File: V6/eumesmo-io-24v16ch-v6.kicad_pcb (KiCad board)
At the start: 4 copper layers, 128 x 67.8 mm, 336 parts, among them J1 250-208, J2 250-208, J3 250-208, J4 250-208, J5 250-202, J6 250-202, J7 USB_C_Receptacle_USB2.0, J8 ETHERNET, J9 250-203, Q1 WPM2015-3/TR, Q10 MMBT2222A, Q11 MMBT2222A, Q12 MMBT2222A, Q13 MMBT2222A, Q14 MMBT2222A, Q15 MMBT2222A, Q16 MMBT2222A, Q17 MMBT2222A, Q18 MMBT2222A, Q19 MMBT2222A, Q2 MMUN2211LT3G, Q3 UMH3N, Q4 MMBT2222A, Q5 MMBT2222A, Q6 MMBT2222A, Q7 MMBT2222A, Q8 MMBT2222A, Q9 MMBT2222A, SW1 RESET, SW2 1WIRE_SEL, U1 TX4138, U10 MCP23017, U11 DS2482S-100, U12 OR-3H7-4, U13 OR-3H7-4, U14 OR-3H7-4, U15 OR-3H7-4, U2 SY8089A1AAC, U3 TPS3820-33, U4 CH340K, U5 ESP32-WROOM-32UE-N16, U6 LAN8710A, U7 TPS3820-33, U8 MCP23008, U9 MCP23008

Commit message: Further improved routing between ETH jack and LAN8710A.
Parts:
- moved R35 3.09 mm to (173.0, 104.1), turned to 180 degrees
- moved R32 3.04 mm to (179.0, 104.1), turned to 0 degrees
- moved C24 1.00 mm to (179.5, 107.1)
- moved R31 0.90 mm to (179.0, 103.1), turned to 0 degrees
- moved R36 0.90 mm to (173.0, 103.1), turned to 180 degrees
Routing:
- net /LAN/ETHRXD-: track 22.8 -> 21.5 mm, vias 1 -> 2
- net +3V3A: track 42.5 -> 43.8 mm, vias 7 -> 6
- net /LAN/ETHTXD+: track 19.2 -> 18.2 mm
- net GND: track 133.3 -> 133.8 mm, vias 142 -> 140

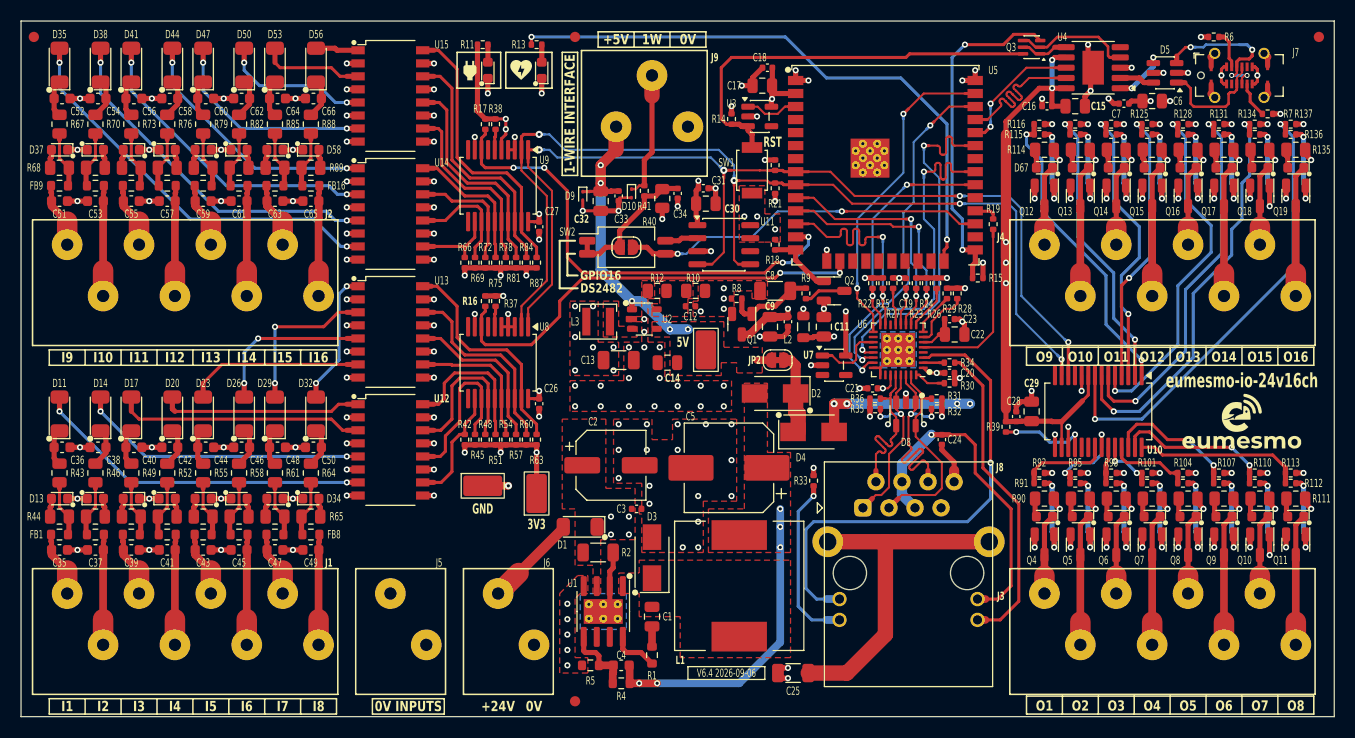
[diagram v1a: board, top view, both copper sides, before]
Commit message: Further improvements to routing between ETH jack and LAN IC.
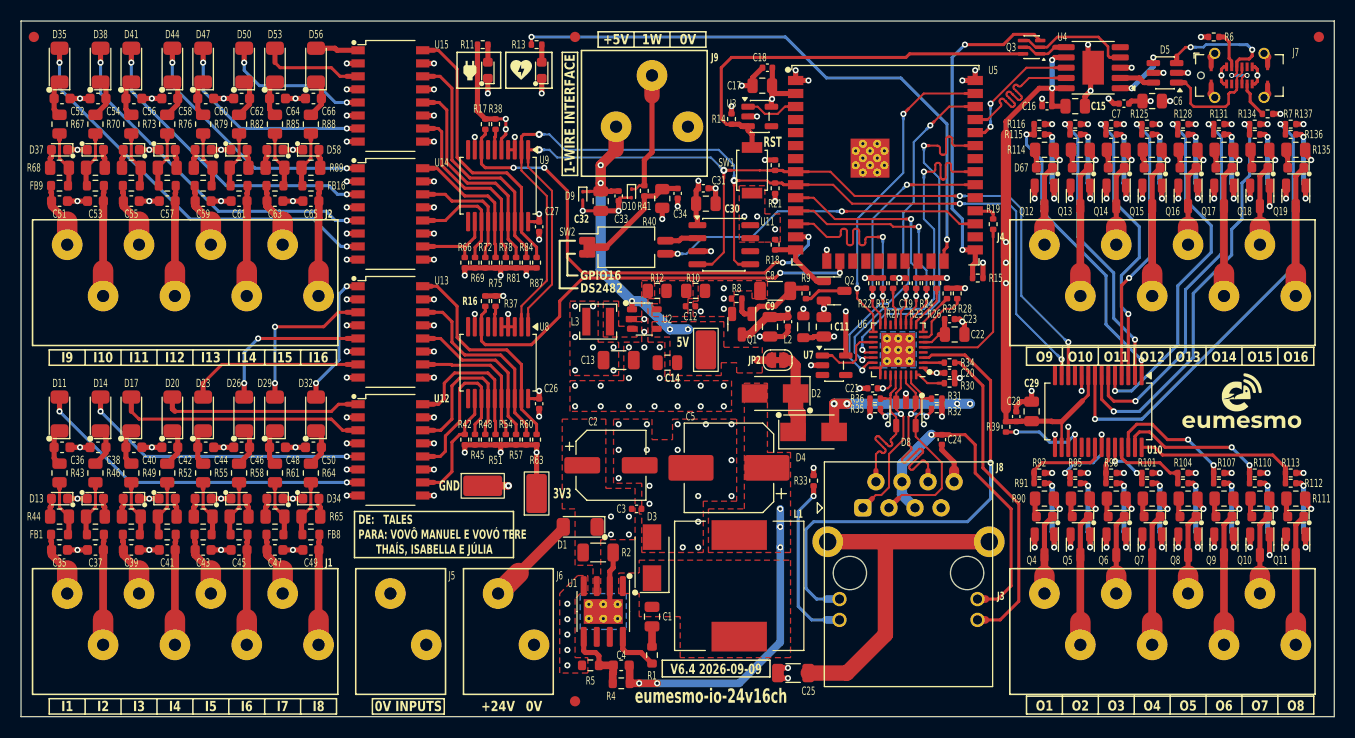
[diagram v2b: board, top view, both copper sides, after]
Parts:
- removed JP1: 1WJUMPER, Jumper:SolderJumper-2_P1.3mm_Open_RoundedPad1.0x1.5mm
- moved G*** 2.00 mm to (208.8, 103.3)
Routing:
- net /I2C Devices/1WIREGPIO: track 35.8 -> 32.4 mm
- net /I2C Devices/1WIREBUS: track 14.1 -> 13.0 mm
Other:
- board text added: "DE: TALES PARA: VOVÔ MANUEL E VOVÓ TERE THAÍS, ISABELLA E JÚLIA"
- board text added: "V6.4 2026-09-09"
- board text removed: "V6.4 2026-09-06"

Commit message: Replaced white leds for emerald.
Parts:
- D13, D16, D19, D22, D25, D28, D31, D34, D37, D40, D43, D46, D49, D52, D55, D58, D59, D6, D60, D61, D62, D63, D64, D65, D66, D67, D68, D69, D7, D70, D71, D72, D73, D74: value WHITE/0603 -> EMERALD/0603
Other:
- board text removed: "DE: TALES PARA: VOVÔ MANUEL E VOVÓ TERE THAÍS, ISABELLA E JÚLIA"
